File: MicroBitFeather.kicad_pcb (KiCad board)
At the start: 2 copper layers, 67.3 x 35.6 mm, 24 parts, among them J1 Feather_Long, J2 Barrel_Jack_MountingPin, J3 Feather_Short, J4 NeoPixels, J5 microbit_edge_connector, U1 74AHCT125, U2 MCP1702-3302E_TO92

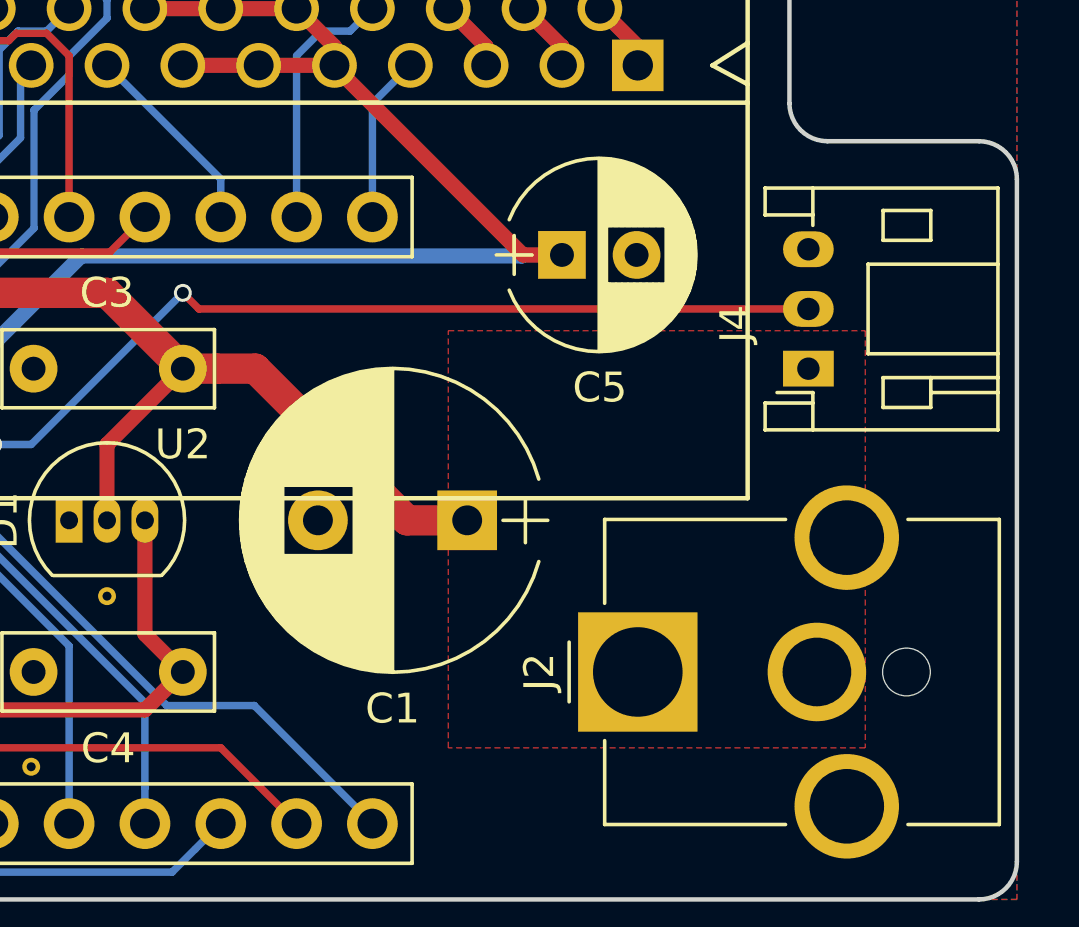
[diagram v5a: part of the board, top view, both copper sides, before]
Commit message: I had the pinout for the NeoPixel connector wrong.
https://cdn.sparkfun.com/datasheets/Prototyping/ACCA-1495.pdf
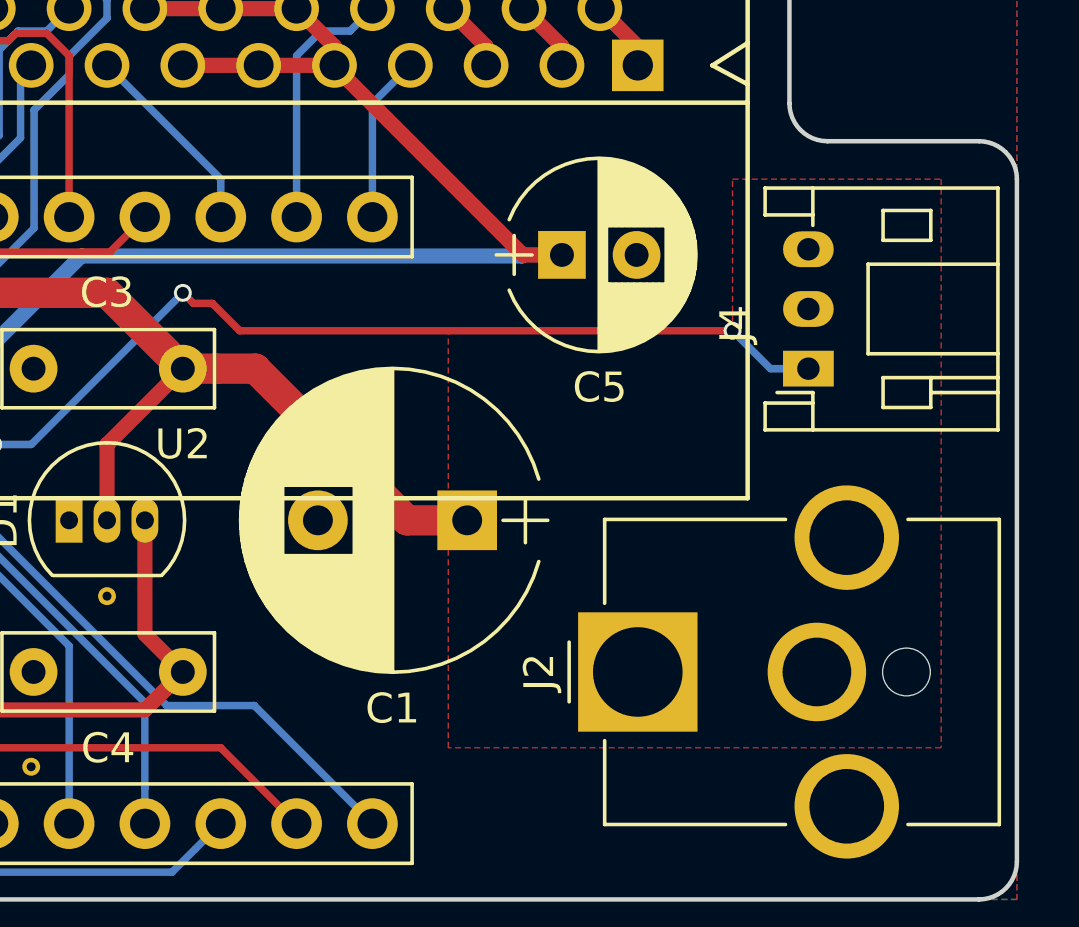
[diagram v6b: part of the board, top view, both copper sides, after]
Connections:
- J4 pad 1: +5V -> Net-(J4-Pad1)
- J4 pad 2: Net-(J4-Pad2) -> GND
- J4 pad 3: GND -> +5V
- R2 pad 2: Net-(J4-Pad2) -> Net-(J4-Pad1)
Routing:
- net Net-(J4-Pad1): track 0.00 -> 41.5 mm, vias 0 -> 5
- net Net-(J4-Pad2): track 40.6 -> 0.00 mm, vias 4 -> 0

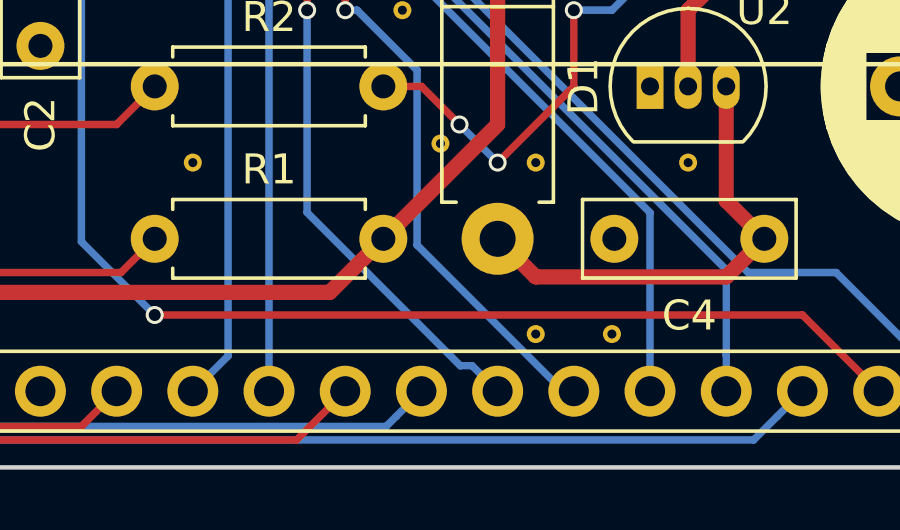
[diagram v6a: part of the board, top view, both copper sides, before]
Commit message: Add a couple more stitching vias, although perhaps I am getting carried away.
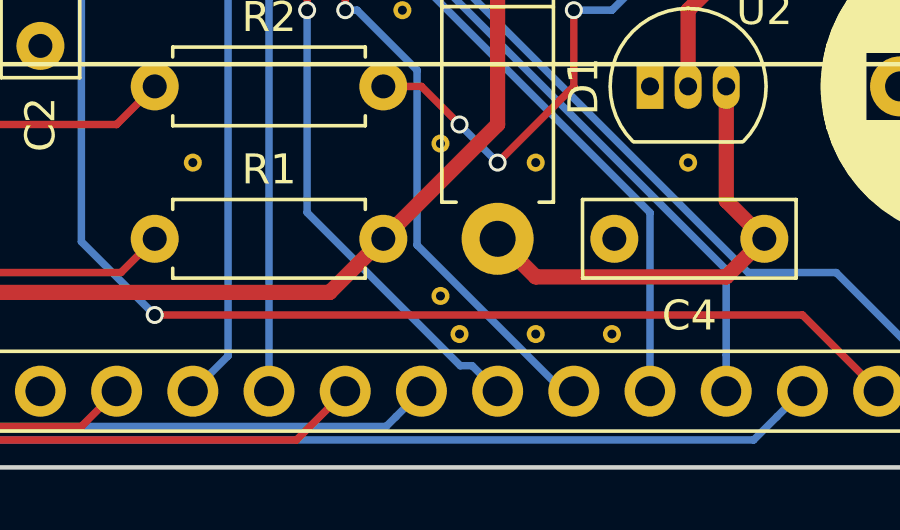
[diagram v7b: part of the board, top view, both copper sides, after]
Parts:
- added VIA: VIA-0.6mm, footprints:VIA-0.6mm, F.Cu at (147.3, 114.9)
- added VIA: VIA-0.6mm, footprints:VIA-0.6mm, F.Cu at (146.7, 113.7)
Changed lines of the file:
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@@
 (kicad_pcb (version 4) (host pcbnew 4.0.7)
   (general
-    (links 87)
+    (links 89)
     (no_connects 0)
     (area 118.034999 79.965 186.795 121.968572)
@@
     (tracks 284)
     (zones 0)
-    (modules 24)
+    (modules 26)
     (nets 72)
   )
@@
   )
   (module footprints:VIA-0.6mm (layer F.Cu)
+    (at 147.32 114.935)
+    (fp_text reference VIA (at 0 0.5) (layer F.SilkS) hide
+      (effects (font (size 0.127 0.127) (thickness 0.015)))
+    )
+    (fp_text value VIA-0.6mm (at 0 -0.5) (layer F.Fab) hide
+      (effects (font (size 0.127 0.127) (thickness 0.015)))
+    )
+    (pad 1 thru_hole circle (at 0 0) (size 0.6 0.6) (drill 0.3) (layers *.Cu)
+      (net 2 GND) (zone_connect 2))
+  )
+  (module footprints:VIA-0.6mm (layer F.Cu)
+    (at 146.685 113.665)
+    (fp_text reference VIA (at 0 0.5) (layer F.SilkS) hide
+      (effects (font (size 0.127 0.127) (thickness 0.015)))
+    )
+    (fp_text value VIA-0.6mm (at 0 -0.5) (layer F.Fab) hide
+      (effects (font (size 0.127 0.127) (thickness 0.015)))
+    )
+    (pad 1 thru_hole circle (at 0 0) (size 0.6 0.6) (drill 0.3) (layers *.Cu)
+      (net 2 GND) (zone_connect 2))
+  )
+  (module footprints:VIA-0.6mm (layer F.Cu)
